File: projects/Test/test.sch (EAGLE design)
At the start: 44 parts, among them J1 284512-3, Y1 ECS-80-S-4X

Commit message: Add motor driver bottom pad and breakout can rx/tx pins
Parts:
- added J12: (no value), SparkFun-Connectors:CONN_02
- U$6: value DRV8340H -> DRV8340HBOTTOM-PAD; device Motor Driver - DRV8340H:DRV8340H -> Motor Driver - DRV8340H:DRV8340HBOTTOM-PAD
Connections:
- new net CAN_RX: J12.2, U$5.PA11
- new net CAN_TX: J12.1, U$5.PA12
- net 12V: now also Q1G$2.D1, Q1G$2.D2; no longer Q1G$1.D1, Q1G$1.D2
- net EN_1: now also U$5.PA15; no longer U$5.PA11
- net FAULT_1: now also U$5.PB3; no longer U$5.PA12
- net GHA_1: now also Q1G$2.G; no longer Q1G$1.G
- net GLA_1: now also Q1G$1.G; no longer Q1G$2.G
- net GND: now also Q1G$1.S; no longer Q1G$2.S
- net N$1: no longer U$5.PB3, U$5.PB4
- net PHASE_A1: now also Q1G$1.D1, Q1G$1.D2, Q1G$2.S; no longer Q1G$1.S, Q1G$2.D1, Q1G$2.D2
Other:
- moved on the sheet: Q1G$1, Q1G$2, U$6G$1
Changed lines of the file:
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@@
 <part name="J6" library="SparkFun-Connectors" library_urn="urn:adsk.eagle:library:513" deviceset="CONN_01" device="" package3d_urn="urn:adsk.eagle:package:38028/1"/>
 <part name="J7" library="SparkFun-Connectors" library_urn="urn:adsk.eagle:library:513" deviceset="CONN_01" device="" package3d_urn="urn:adsk.eagle:package:38028/1"/>
-<part name="U$6" library="Motor Driver - DRV8340H" deviceset="DRV8340H" device=""/>
+<part name="U$6" library="Motor Driver - DRV8340H" deviceset="DRV8340H" device="BOTTOM-PAD"/>
 <part name="GND4" library="SparkFun-PowerSymbols" library_urn="urn:adsk.eagle:library:530" deviceset="GND" device=""/>
 <part name="GND5" library="SparkFun-PowerSymbols" library_urn="urn:adsk.eagle:library:530" deviceset="GND" device=""/>
@@
 <part name="J10" library="SparkFun-Connectors" library_urn="urn:adsk.eagle:library:513" deviceset="BANANA_CONN" device="" package3d_urn="urn:adsk.eagle:package:38018/1"/>
 <part name="J11" library="SparkFun-Connectors" library_urn="urn:adsk.eagle:library:513" deviceset="BANANA_CONN" device="" package3d_urn="urn:adsk.eagle:package:38018/1"/>
+<part name="J12" library="SparkFun-Connectors" library_urn="urn:adsk.eagle:library:513" deviceset="CONN_02" device="" package3d_urn="urn:adsk.eagle:package:38039/1"/>
 </parts>
 <sheets>
@@
 <attribute name="NAME" x="111.76" y="13.208" size="1.778" layer="95" font="vector"/>
 </instance>
+<instance part="J12" gate="G$1" x="38.1" y="66.04" smashed="yes">
+<attribute name="VALUE" x="35.56" y="61.214" size="1.778" layer="96" font="vector"/>
+<attribute name="NAME" x="35.56" y="71.628" size="1.778" layer="95" font="vector"/>
+</instance>
 </instances>
 <busses>
@@
 <net name="N$1" class="0">
 <segment>
-<pinref part="U$5" gate="G$1" pin="PB3"/>
-<wire x1="139.7" y1="88.9" x2="142.24" y2="88.9" width="0.1524" layer="91"/>
-<wire x1="142.24" y1="88.9" x2="142.24" y2="86.36" width="0.1524" layer="91"/>
-<pinref part="U$5" gate="G$1" pin="PB4"/>
-<wire x1="142.24" y1="86.36" x2="139.7" y2="86.36" width="0.1524" layer="91"/>
 <pinref part="U$5" gate="G$1" pin="PB5"/>
 <wire x1="139.7" y1="83.82" x2="142.24" y2="83.82" width="0.1524" layer="91"/>
-<wire x1="142.24" y1="83.82" x2="142.24" y2="86.36" width="0.1524" layer="91"/>
-<junction x="142.24" y="86.36"/>
 <pinref part="U$5" gate="G$1" pin="PB6"/>
 <wire x1="139.7" y1="81.28" x2="142.24" y2="81.28" width="0.1524" layer="91"/>
 <wire x1="142.24" y1="81.28" x2="142.24" y2="83.82" width="0.1524" layer="91"/>
-<junction x="142.24" y="83.82"/>
 </segment>
 </net>
 <net name="EN_1" class="0">
 <segment>
+<wire x1="91.44" y1="58.42" x2="93.98" y2="58.42" width="0.1524" layer="91"/>
+<label x="91.44" y="58.42" size="1.27" layer="95" rot="R180" xref="yes"/>
+<pinref part="U$5" gate="G$1" pin="PA15"/>
+</segment>
+</net>
+<net name="FAULT_1" class="0">
+<segment>
+<wire x1="139.7" y1="88.9" x2="142.24" y2="88.9" width="0.1524" layer="91"/>
+<label x="142.24" y="88.9" size="1.27" layer="95" rot="MR180" xref="yes"/>
+<pinref part="U$5" gate="G$1" pin="PB3"/>
+</segment>
+</net>
+<net name="CAN_RX" class="0">
+<segment>
 <pinref part="U$5" gate="G$1" pin="PA11"/>
-<wire x1="91.44" y1="68.58" x2="93.98" y2="68.58" width="0.1524" layer="91"/>
+<wire x1="93.98" y1="68.58" x2="91.44" y2="68.58" width="0.1524" layer="91"/>
 <label x="91.44" y="68.58" size="1.27" layer="95" rot="R180" xref="yes"/>
 </segment>
-</net>
-<net name="FAULT_1" class="0">
+<segment>
+<wire x1="45.72" y1="68.58" x2="48.26" y2="68.58" width="0.1524" layer="91"/>
+<label x="48.26" y="68.58" size="1.27" layer="95" rot="MR180" xref="yes"/>
+<pinref part="J12" gate="G$1" pin="2"/>
+</segment>
+</net>
+<net name="CAN_TX" class="0">
 <segment>
 <pinref part="U$5" gate="G$1" pin="PA12"/>
-<wire x1="93.98" y1="66.04" x2="91.44" y2="66.04" width="0.1524" layer="91"/>
+<wire x1="91.44" y1="66.04" x2="93.98" y2="66.04" width="0.1524" layer="91"/>
 <label x="91.44" y="66.04" size="1.27" layer="95" rot="R180" xref="yes"/>
+</segment>
+<segment>
+<wire x1="48.26" y1="66.04" x2="45.72" y2="66.04" width="0.1524" layer="91"/>
+<label x="48.26" y="66.04" size="1.27" layer="95" rot="MR180" xref="yes"/>
+<pinref part="J12" gate="G$1" pin="1"/>
 </segment>
 </net>
@@
 <attribute name="VALUE" x="50.8" y="86.106" size="1.778" layer="96" align="top-center"/>
 </instance>
-<instance part="Q1" gate="G$1" x="55.88" y="63.5" smashed="yes">
+<instance part="Q1" gate="G$2" x="55.88" y="63.5" smashed="yes">
 <attribute name="NAME" x="60.96" y="63.5" size="1.778" layer="95" font="vector"/>
 <attribute name="VALUE" x="60.96" y="60.96" size="1.778" layer="96" font="vector"/>
 </instance>
-<instance part="Q1" gate="G$2" x="55.88" y="30.48" smashed="yes">
+<instance part="Q1" gate="G$1" x="55.88" y="30.48" smashed="yes">
 <attribute name="NAME" x="60.96" y="30.48" size="1.778" layer="95" font="vector"/>
 <attribute name="VALUE" x="60.96" y="27.94" size="1.778" layer="96" font="vector"/>
@@
 <net name="GLA_1" class="0">
 <segment>
-<pinref part="Q1" gate="G$2" pin="G"/>
+<pinref part="Q1" gate="G$1" pin="G"/>
 <wire x1="50.8" y1="27.94" x2="48.26" y2="27.94" width="0.1524" layer="91"/>
 <label x="48.26" y="27.94" size="1.778" layer="95" rot="R180" xref="yes"/>
@@
 </segment>
 <segment>
-<pinref part="Q1" gate="G$1" pin="D1"/>
+<pinref part="Q1" gate="G$2" pin="D1"/>
 <wire x1="58.42" y1="68.58" x2="58.42" y2="71.12" width="0.1524" layer="91"/>
 <label x="58.42" y="71.12" size="1.778" layer="95" xref="yes"/>
-<pinref part="Q1" gate="G$1" pin="D2"/>
+<pinref part="Q1" gate="G$2" pin="D2"/>
 <wire x1="55.88" y1="68.58" x2="58.42" y2="68.58" width="0.1524" layer="91"/>
 <junction x="58.42" y="68.58"/>
@@
 </segment>
 <segment>
-<pinref part="Q1" gate="G$2" pin="S"/>
+<pinref part="Q1" gate="G$1" pin="S"/>
 <wire x1="58.42" y1="25.4" x2="58.42" y2="22.86" width="0.1524" layer="91"/>
 <pinref part="GND16" gate="1" pin="GND"/>
@@
 <net name="GHA_1" class="0">
 <segment>
-<pinref part="Q1" gate="G$1" pin="G"/>
+<pinref part="Q1" gate="G$2" pin="G"/>
 <wire x1="50.8" y1="60.96" x2="48.26" y2="60.96" width="0.1524" layer="91"/>
 <label x="48.26" y="60.96" size="1.778" layer="95" rot="R180" xref="yes"/>
@@
 <segment>
 <label x="43.18" y="50.8" size="1.778" layer="95" rot="R180" xref="yes"/>
-<pinref part="Q1" gate="G$1" pin="S"/>
-<pinref part="Q1" gate="G$2" pin="D1"/>
+<pinref part="Q1" gate="G$2" pin="S"/>
+<pinref part="Q1" gate="G$1" pin="D1"/>
 <wire x1="58.42" y1="58.42" x2="58.42" y2="50.8" width="0.1524" layer="91"/>
 <wire x1="58.42" y1="50.8" x2="58.42" y2="45.72" width="0.1524" layer="91"/>
@@
 <label x="60.96" y="45.72" size="1.778" layer="95" xref="yes"/>
 <junction x="58.42" y="50.8"/>
-<pinref part="Q1" gate="G$2" pin="D2"/>
+<pinref part="Q1" gate="G$1" pin="D2"/>
 <wire x1="55.88" y1="35.56" x2="58.42" y2="35.56" width="0.1524" layer="91"/>
 <junction x="58.42" y="35.56"/>

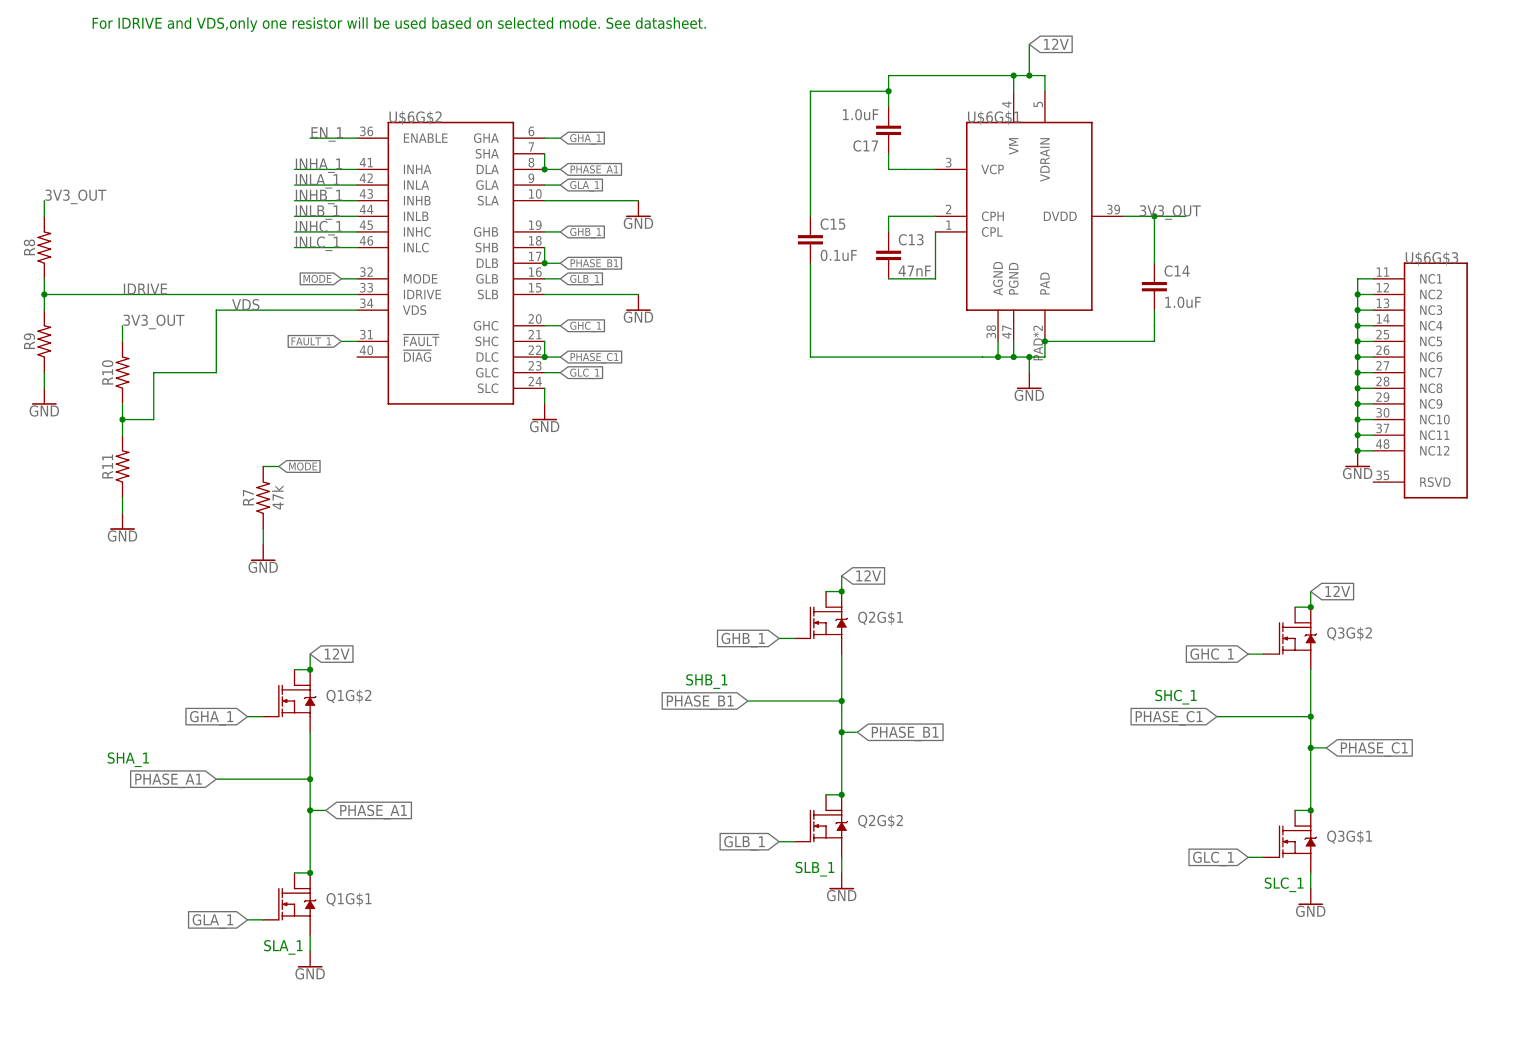
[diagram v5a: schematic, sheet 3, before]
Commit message: Switch to drv8343
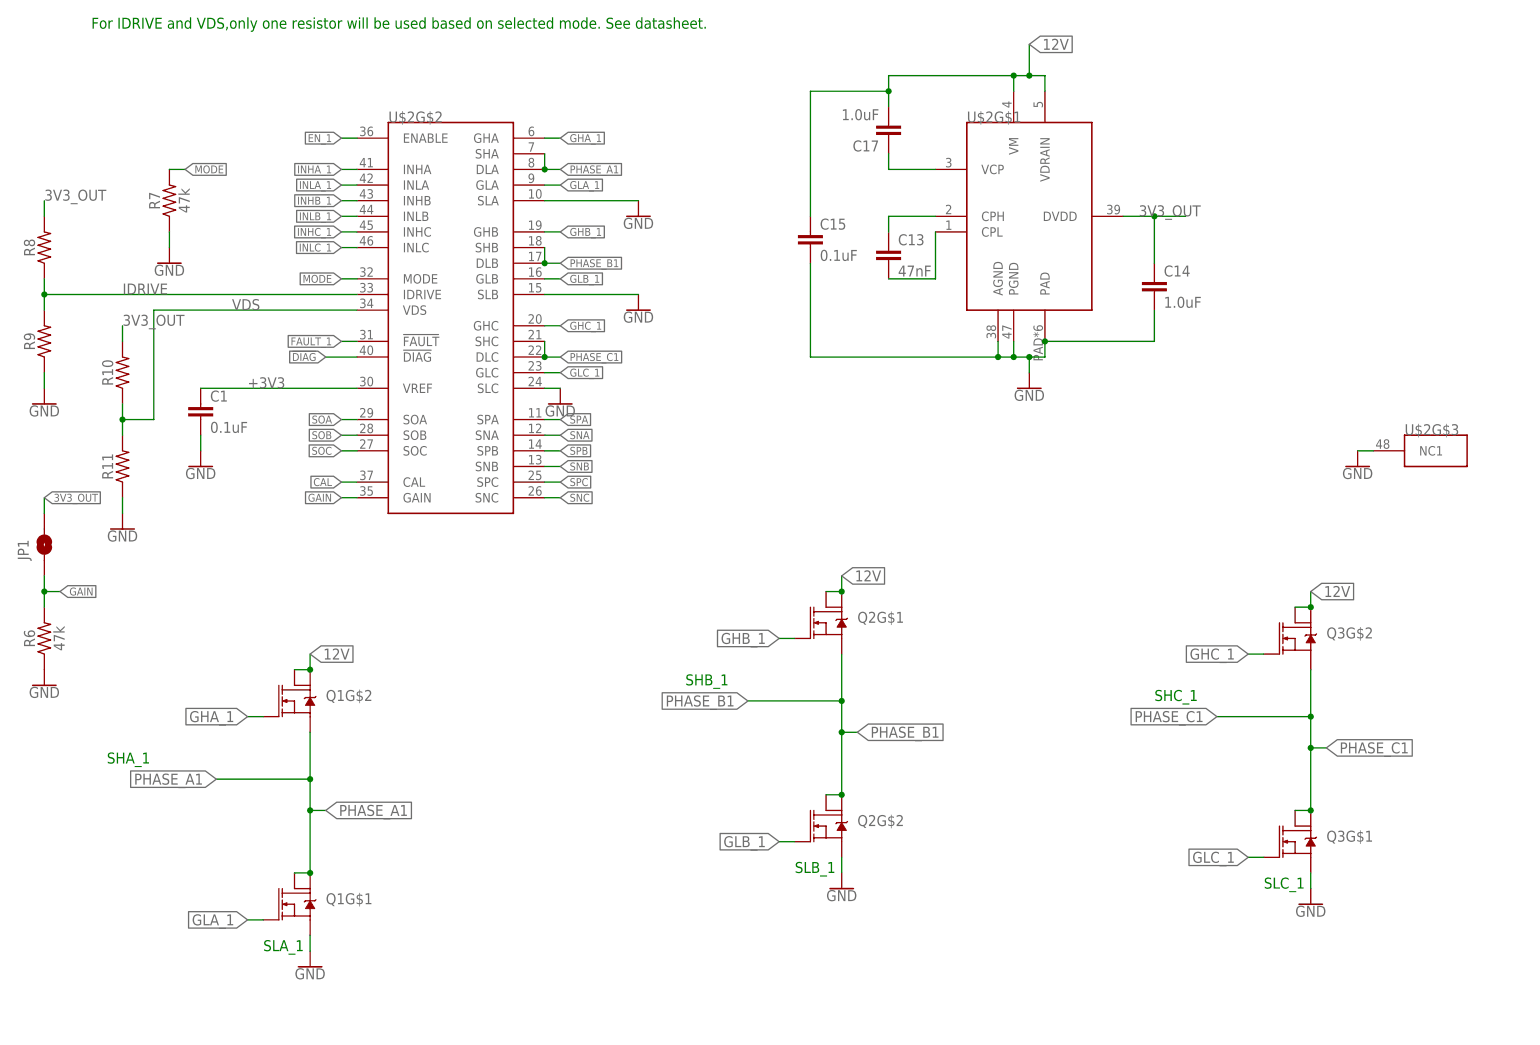
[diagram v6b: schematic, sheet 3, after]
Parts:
- removed U$6: DRV8340HBOTTOM-PAD, Motor Driver - DRV8340H:DRV8340HBOTTOM-PAD
- added C1: 0.1uF, SparkFun-Capacitors:0.1UF-0603-25V-(+80/-20%)
- added JP1: JUMPER-SMT_2_NO_NO-SILK, SparkFun-Jumpers:JUMPER-SMT_2_NO_NO-SILK
- added R6: 47k, SparkFun-Resistors:47KOHM-0603-1/10W-1%
- added U$2: DRV8343H, Motor Driver - DRV834xH:DRV8343H
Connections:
- new net !DIAG: U$2G$2.!DIAG
- new net CAL: U$2G$2.CAL, U$5.PB4
- new net GAIN: JP1.1, R6.2, U$2G$2.GAIN
- new net SNA: U$2G$2.SNA
- new net SNB: U$2G$2.SNB
- new net SNC: U$2G$2.SNC
- new net SOA: U$2G$2.SOA, U$5.PA2
- new net SOB: U$2G$2.SOB, U$5.PA3
- new net SOC: U$2G$2.SOC, U$5.PA5
- new net SPA: U$2G$2.SPA
- new net SPB: U$2G$2.SPB
- new net SPC: U$2G$2.SPC
- net +3V3: now also C1.1, U$2G$2.VREF
- net 12V: now also U$2G$1.VDRAIN, U$2G$1.VM; no longer U$6G$1.VDRAIN, U$6G$1.VM
- net 3V3_OUT: now also JP1.2, U$2G$1.DVDD; no longer U$6G$1.DVDD
- net CPH: now also U$2G$1.CPH; no longer U$6G$1.CPH
- net CPL: now also U$2G$1.CPL; no longer U$6G$1.CPL
- net EN_1: now also U$2G$2.ENABLE; no longer U$6G$2.ENABLE
- net FAULT_1: now also U$2G$2.!FAULT; no longer U$6G$2.!FAULT
- net GHA_1: now also U$2G$2.GHA; no longer U$6G$2.GHA
- net GHB_1: now also U$2G$2.GHB; no longer U$6G$2.GHB
- net GHC_1: now also U$2G$2.GHC; no longer U$6G$2.GHC
- net GLA_1: now also U$2G$2.GLA; no longer U$6G$2.GLA
- net GLB_1: now also U$2G$2.GLB; no longer U$6G$2.GLB
- net GLC_1: now also U$2G$2.GLC; no longer U$6G$2.GLC
- net GND: now also C1.2, R6.1, U$2G$1.AGND, U$2G$1.PAD, U$2G$1.PGND, U$2G$2.SLA, U$2G$2.SLB, U$2G$2.SLC, U$2G$3.NC1; no longer U$6G$1.AGND, U$6G$1.PAD, U$6G$1.PGND, U$6G$2.SLA, U$6G$2.SLB, U$6G$2.SLC, U$6G$3.NC1, U$6G$3.NC10, U$6G$3.NC11, U$6G$3.NC12, U$6G$3.NC2, U$6G$3.NC3, U$6G$3.NC4, U$6G$3.NC5, U$6G$3.NC6, U$6G$3.NC7, U$6G$3.NC8, U$6G$3.NC9
- net IDRIVE: now also U$2G$2.IDRIVE; no longer U$6G$2.IDRIVE
- net INHA_1: now also U$2G$2.INHA; no longer U$6G$2.INHA
- net INHB_1: now also U$2G$2.INHB; no longer U$6G$2.INHB
- net INHC_1: now also U$2G$2.INHC; no longer U$6G$2.INHC
- net INLA_1: now also U$2G$2.INLA; no longer U$6G$2.INLA
- net INLB_1: now also U$2G$2.INLB; no longer U$6G$2.INLB
- net INLC_1: now also U$2G$2.INLC; no longer U$6G$2.INLC
- net MODE: now also U$2G$2.MODE; no longer U$6G$2.MODE
- net PHASE_A1: now also U$2G$2.DLA, U$2G$2.SHA; no longer U$6G$2.DLA, U$6G$2.SHA
- net PHASE_B1: now also U$2G$2.DLB, U$2G$2.SHB; no longer U$6G$2.DLB, U$6G$2.SHB
- net PHASE_C1: now also U$2G$2.DLC, U$2G$2.SHC; no longer U$6G$2.DLC, U$6G$2.SHC
- net VDS: now also U$2G$2.VDS; no longer U$6G$2.VDS
- net V_CAP_L: now also U$2G$1.VCP; no longer U$6G$1.VCP
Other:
- moved on the sheet: R7

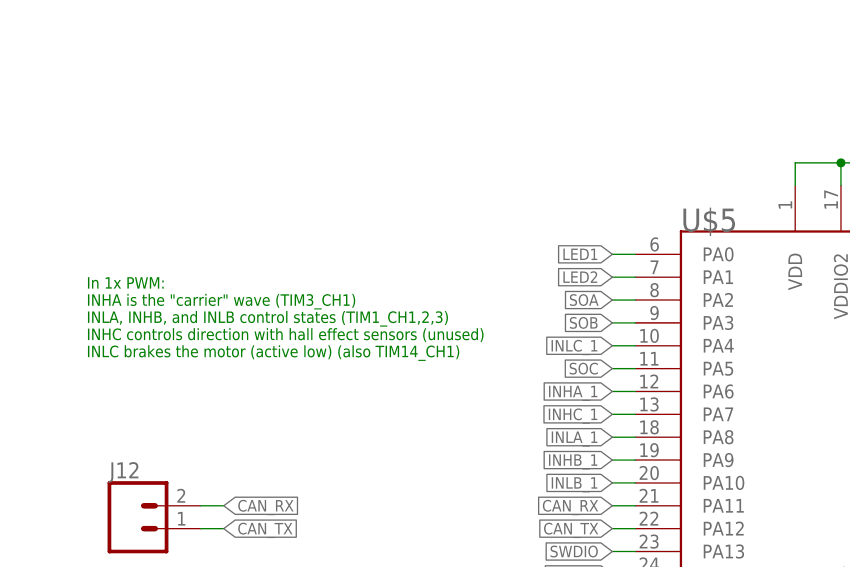
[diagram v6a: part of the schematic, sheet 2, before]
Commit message: Use no thermal banana con part. Remove DS Store
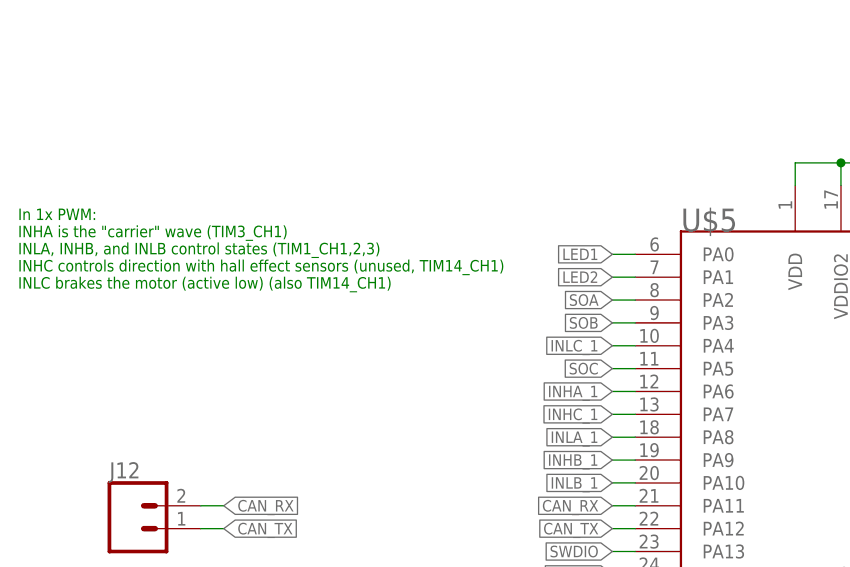
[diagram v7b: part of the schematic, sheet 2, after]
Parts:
- J10, J11: device SparkFun-Connectors:BANANA_CONN -> Banana Plug PTH:BANANA_PTH
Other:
- note added: "In 1x PWM: INHA is the "carrier" wave (TIM3_CH1) INLA, INHB, and INLB control states (TIM1_CH1,2,3) INHC controls direction with hall effect sensors (unused, TIM14_CH1) INLC brakes the motor (active low) (also TIM14_CH1)"
- note removed: "In 1x PWM: INHA is the "carrier" wave (TIM3_CH1) INLA, INHB, and INLB control states (TIM1_CH1,2,3) INHC controls direction with hall effect sensors (unused) INLC brakes the motor (active low) (also TIM14_CH1)"
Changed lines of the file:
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@@
 <part name="J8" library="SparkFun-Connectors" library_urn="urn:adsk.eagle:library:513" deviceset="CONN_01" device="" package3d_urn="urn:adsk.eagle:package:38028/1"/>
 <part name="J9" library="SparkFun-Connectors" library_urn="urn:adsk.eagle:library:513" deviceset="CONN_01" device="" package3d_urn="urn:adsk.eagle:package:38028/1"/>
-<part name="J10" library="SparkFun-Connectors" library_urn="urn:adsk.eagle:library:513" deviceset="BANANA_CONN" device="" package3d_urn="urn:adsk.eagle:package:38018/1"/>
-<part name="J11" library="SparkFun-Connectors" library_urn="urn:adsk.eagle:library:513" deviceset="BANANA_CONN" device="" package3d_urn="urn:adsk.eagle:package:38018/1"/>
+<part name="J10" library="Banana Plug PTH" deviceset="BANANA_PTH" device=""/>
+<part name="J11" library="Banana Plug PTH" deviceset="BANANA_PTH" device=""/>
 <part name="J12" library="SparkFun-Connectors" library_urn="urn:adsk.eagle:library:513" deviceset="CONN_02" device="" package3d_urn="urn:adsk.eagle:package:38039/1"/>
 <part name="U$2" library="Motor Driver - DRV834xH" deviceset="DRV8343H" device=""/>
@@
 <text x="111.76" y="154.94" size="1.778" layer="91">Pin 1 (VBAT)</text>
 <text x="132.08" y="154.94" size="1.778" layer="91">Pin 13 (VDDA)</text>
-<text x="33.02" y="93.98" size="1.27" layer="91" align="top-left">In 1x PWM:
+<text x="25.4" y="101.6" size="1.27" layer="91" align="top-left">In 1x PWM:
 INHA is the "carrier" wave (TIM3_CH1)
 INLA, INHB, and INLB control states (TIM1_CH1,2,3)
-INHC controls direction with hall effect sensors (unused)
+INHC controls direction with hall effect sensors (unused, TIM14_CH1)
 INLC brakes the motor (active low) (also TIM14_CH1)</text>
 </plain>
